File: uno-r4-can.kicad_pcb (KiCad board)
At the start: 2 copper layers, 68.6 x 53.3 mm, 21 parts, among them J101 CANOpen, J102 Power, J103 Analog, J104 Digital/PWM, J105 Digital/PWM, U101 L78L05_SOT89, U102 ISO1050DUB

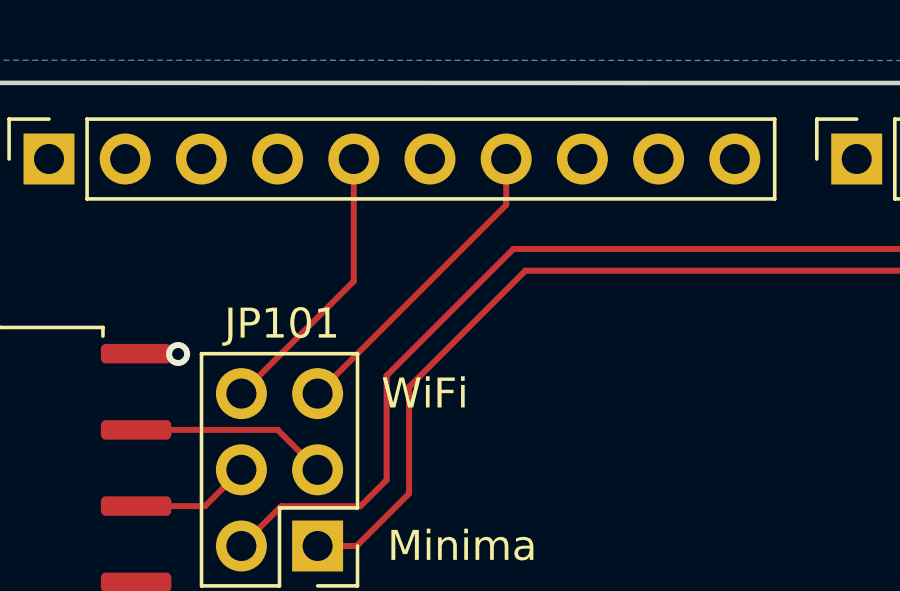
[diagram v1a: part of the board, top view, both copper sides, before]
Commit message: Wifi TX is on pin 10
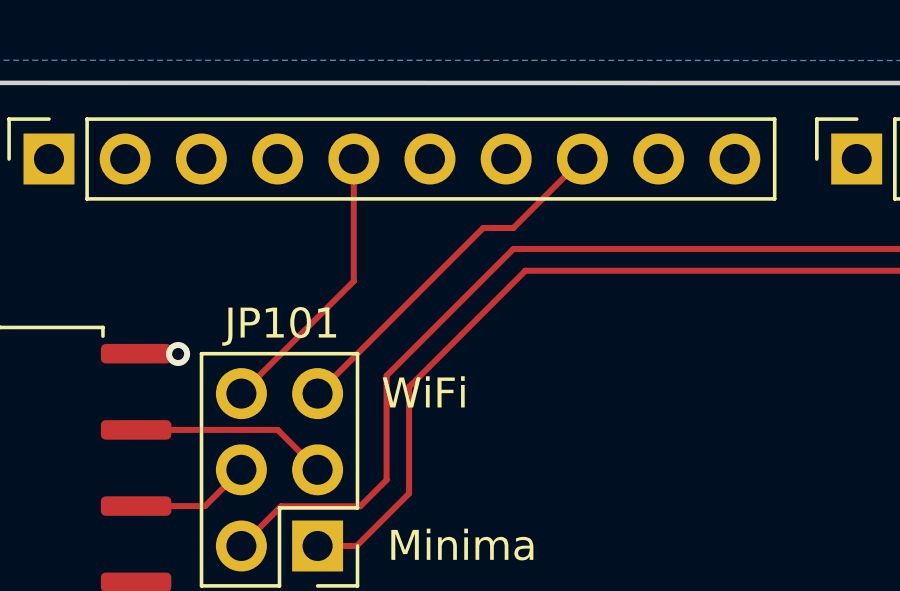
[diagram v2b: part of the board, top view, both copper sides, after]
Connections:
- net /SCL/A5 renamed /SCL
- net /SDA/A4 renamed /SDA
- J103 pad 5: unconnected-(J103-Pin_5-Pad5) -> /A4
- J103 pad 6: unconnected-(J103-Pin_6-Pad6) -> /A5
- JP101 pad 5: /~11 -> /~10
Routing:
- net /~10: track 0.00 -> 12.1 mm
- net /~11: track 10.4 -> 0.00 mm
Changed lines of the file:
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@@
   (net 7 "/A2")
   (net 8 "/A3")
-  (net 9 "/SDA{slash}A4")
-  (net 10 "/SCL{slash}A5")
+  (net 9 "/A4")
+  (net 10 "/A5")
   (net 11 "/12")
   (net 12 "/AREF")
@@
   (net 37 "VCAN")
   (net 38 "unconnected-(J102-Pin_1-Pad1)")
-  (net 39 "unconnected-(J103-Pin_5-Pad5)")
-  (net 40 "unconnected-(J103-Pin_6-Pad6)")
+  (net 39 "/SCL")
+  (net 40 "/SDA")
   (footprint "Connector_PinSocket_2.54mm:PinSocket_1x08_P2.54mm_Vertical" locked (layer "F.Cu")
     (at 127.94 97.46 90)
@@
       (net 8 "/A3") (pinfunction "Pin_4") (pintype "passive+no_connect"))
     (pad "5" thru_hole oval locked (at 0 10.16 90) (size 1.7 1.7) (drill 1) (layers "*.Cu" "*.Mask")
-      (net 39 "unconnected-(J103-Pin_5-Pad5)") (pinfunction "Pin_5") (pintype "passive+no_connect"))
+      (net 9 "/A4") (pinfunction "Pin_5") (pintype "passive+no_connect"))
     (pad "6" thru_hole oval locked (at 0 12.7 90) (size 1.7 1.7) (drill 1) (layers "*.Cu" "*.Mask")
-      (net 40 "unconnected-(J103-Pin_6-Pad6)") (pinfunction "Pin_6") (pintype "passive+no_connect"))
+      (net 10 "/A5") (pinfunction "Pin_6") (pintype "passive+no_connect"))
     (model "${KICAD6_3DMODEL_DIR}/Connector_PinSocket_2.54mm.3dshapes/PinSocket_1x06_P2.54mm_Vertical.wrl"
       (offset (xyz 0 0 0))
@@
       (stroke (width 0.1) (type solid)) (layer "F.Fab"))
     (pad "1" thru_hole rect locked (at 0 0 90) (size 1.7 1.7) (drill 1) (layers "*.Cu" "*.Mask")
-      (net 10 "/SCL{slash}A5") (pinfunction "Pin_1") (pintype "passive+no_connect"))
+      (net 39 "/SCL") (pinfunction "Pin_1") (pintype "passive+no_connect"))
     (pad "2" thru_hole oval locked (at 0 2.54 90) (size 1.7 1.7) (drill 1) (layers "*.Cu" "*.Mask")
-      (net 9 "/SDA{slash}A4") (pinfunction "Pin_2") (pintype "passive+no_connect"))
+      (net 40 "/SDA") (pinfunction "Pin_2") (pintype "passive+no_connect"))
     (pad "3" thru_hole oval locked (at 0 5.08 90) (size 1.7 1.7) (drill 1) (layers "*.Cu" "*.Mask")
       (net 12 "/AREF") (pinfunction "Pin_3") (pintype "passive+no_connect"))
@@
       (net 11 "/12") (pinfunction "Pin_6") (pintype "passive+no_connect"))
     (pad "7" thru_hole oval locked (at 0 15.24 90) (size 1.7 1.7) (drill 1) (layers "*.Cu" "*.Mask")
-      (net 29 "/~11") (pinfunction "Pin_7") (pintype "passive"))
+      (net 29 "/~11") (pinfunction "Pin_7") (pintype "passive+no_connect"))
     (pad "8" thru_hole oval locked (at 0 17.78 90) (size 1.7 1.7) (drill 1) (layers "*.Cu" "*.Mask")
-      (net 30 "/~10") (pinfunction "Pin_8") (pintype "passive+no_connect"))
+      (net 30 "/~10") (pinfunction "Pin_8") (pintype "passive"))
     (pad "9" thru_hole oval locked (at 0 20.32 90) (size 1.7 1.7) (drill 1) (layers "*.Cu" "*.Mask")
       (net 31 "/~9") (pinfunction "Pin_9") (pintype "passive+no_connect"))
@@
       (net 26 "/CAN_RX") (pinfunction "Pin_4") (pintype "passive"))
     (pad "5" thru_hole oval (at 0 5.08 180) (size 1.7 1.7) (drill 1) (layers "*.Cu" "*.Mask")
-      (net 29 "/~11") (pinfunction "Pin_5") (pintype "passive"))
+      (net 30 "/~10") (pinfunction "Pin_5") (pintype "passive"))
     (pad "6" thru_hole oval (at 2.54 5.08 180) (size 1.7 1.7) (drill 1) (layers "*.Cu" "*.Mask")
       (net 28 "/13") (pinfunction "Pin_6") (pintype "passive"))
@@
   (segment (start 125.21 57.02) (end 128.956 53.274) (width 0.2) (layer "F.Cu") (net 28))
   (segment (start 128.956 53.274) (end 128.956 49.2) (width 0.2) (layer "F.Cu") (net 28))
-  (segment (start 127.75 57.02) (end 134.036 50.734) (width 0.2) (layer "F.Cu") (net 29))
-  (segment (start 134.036 50.734) (end 134.036 49.2) (width 0.2) (layer "F.Cu") (net 29))
+  (segment (start 133.27 51.5) (end 134.276 51.5) (width 0.2) (layer "F.Cu") (net 30))
+  (segment (start 134.276 51.5) (end 136.576 49.2) (width 0.2) (layer "F.Cu") (net 30))
+  (segment (start 127.75 57.02) (end 133.27 51.5) (width 0.2) (layer "F.Cu") (net 30))
   (segment (start 129.175 60.775) (end 130.05 59.9) (width 0.2) (layer "F.Cu") (net 33))
   (segment (start 134.275 52.2) (end 147.8 52.2) (width 0.2) (layer "F.Cu") (net 33))
